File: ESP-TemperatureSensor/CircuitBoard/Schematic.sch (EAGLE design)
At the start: 12 parts

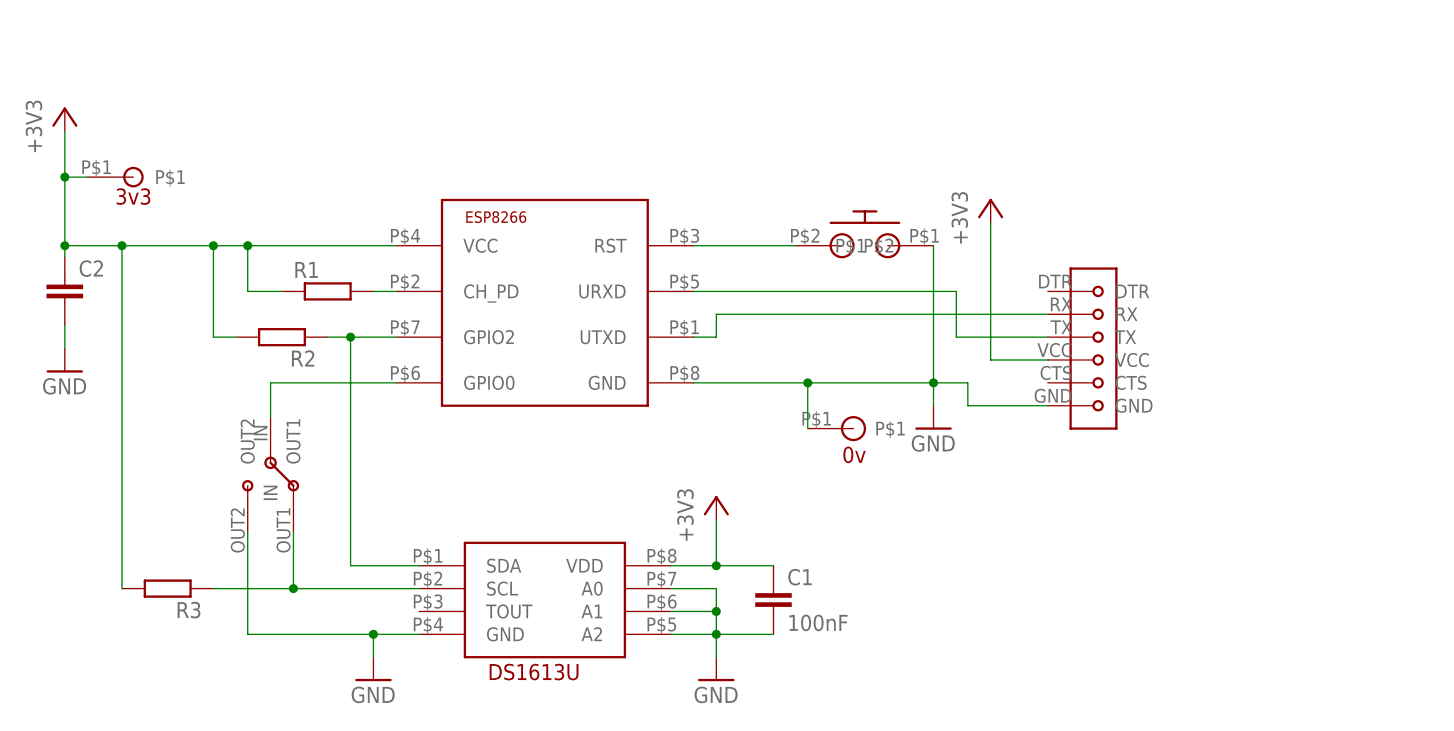
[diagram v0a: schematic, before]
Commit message: Updated the circuit
Updated the circuit diagram and created a better single sided PCB design
for prototyping.
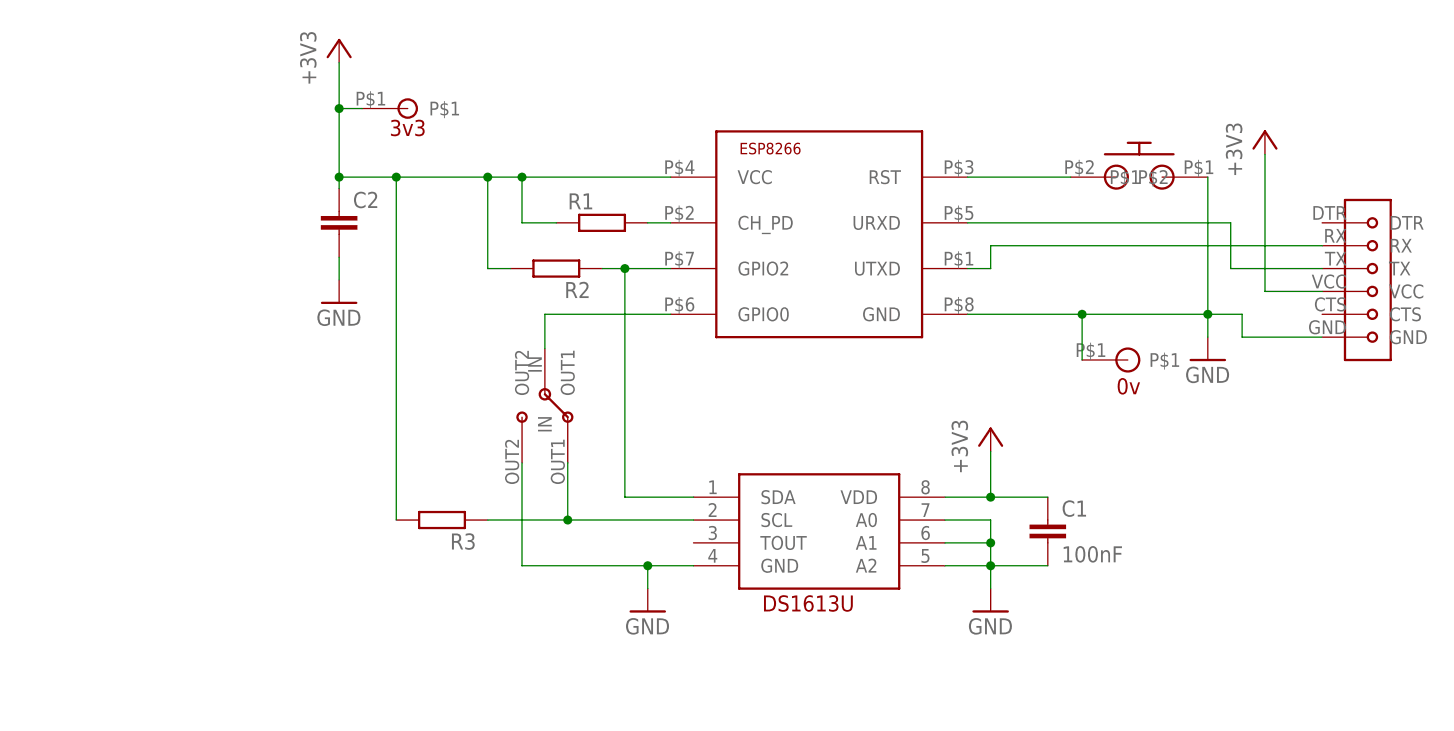
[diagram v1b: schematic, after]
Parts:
- C1, C2: device rcl:C-EU025-025X050 -> rcl:C-EUC0603
- R1, R2, R3: device rcl:R-EU_0207/10 -> rcl:R-EU_R0603
- U$3: value DS1631U-BREAKOUT -> DS1631U+; device ICs:DS1631U-BREAKOUT -> ICs:DS1631U+
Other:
- moved on the sheet: C1, C2, R1, R2, R3
